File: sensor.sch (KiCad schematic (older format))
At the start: 74 parts, among them CON1 Micro USB, CON2 PROG, CON3 Jack-DC, CON4 HTU21D, CON5 N.C., Q1 BSS214N, Q2 BSS214N, Q3 BSS214N, SW1 RESET, SW2 CFG, U1 LM7805, U2 TLV1117LV33DCY, U3 ESP-12F, U4 HTU21D, U5 PMS7003

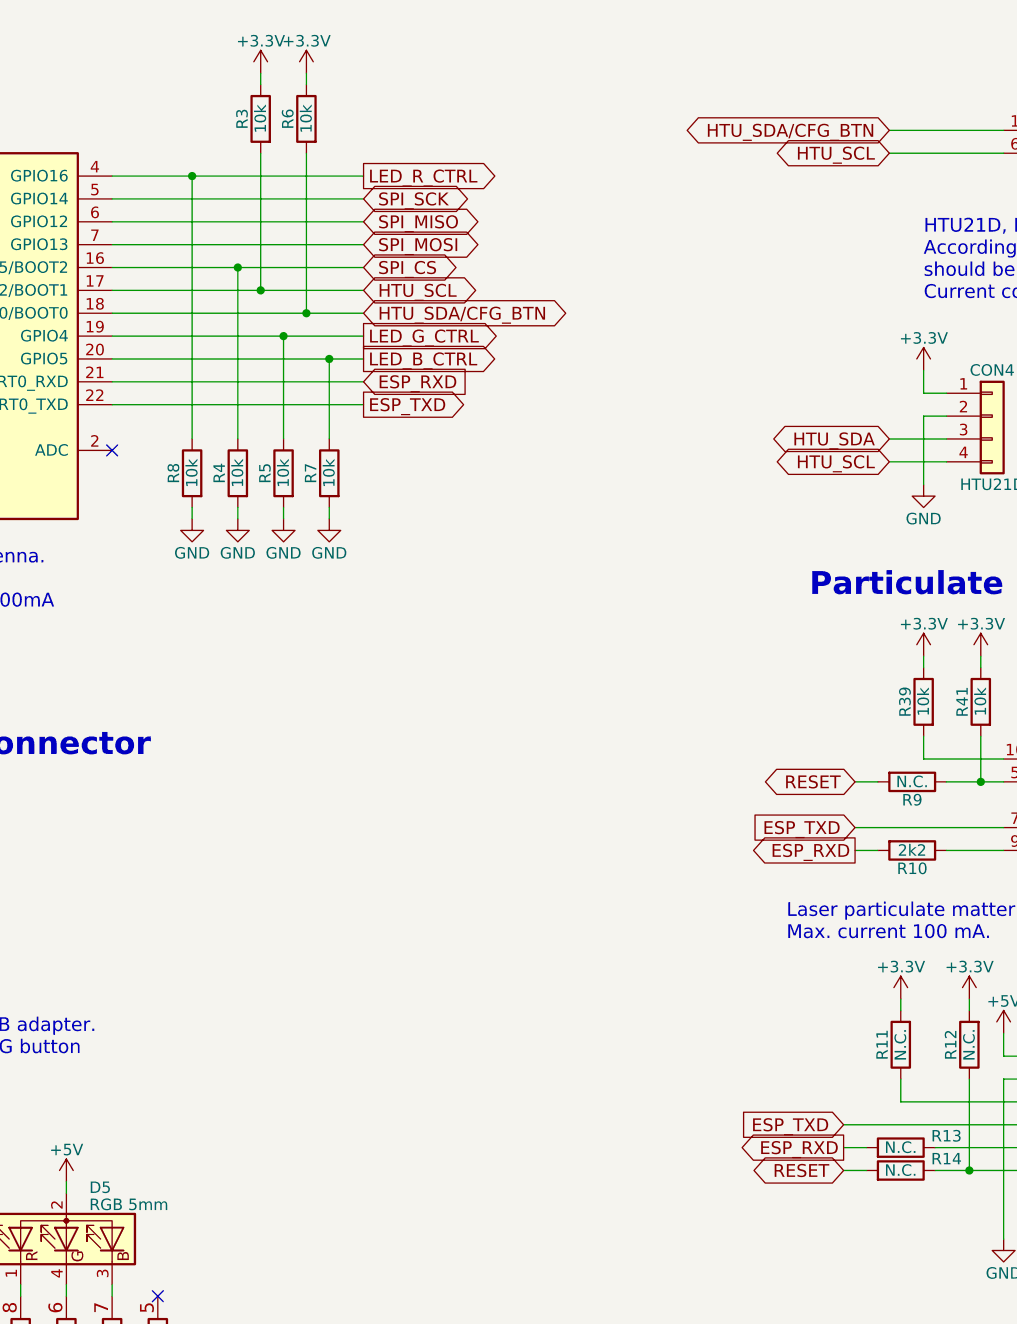
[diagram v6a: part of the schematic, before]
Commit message: Go back to previous ESP pinout, except I2C and LED_B_CTRL [#6] Hardware SPI for Lora module not available.
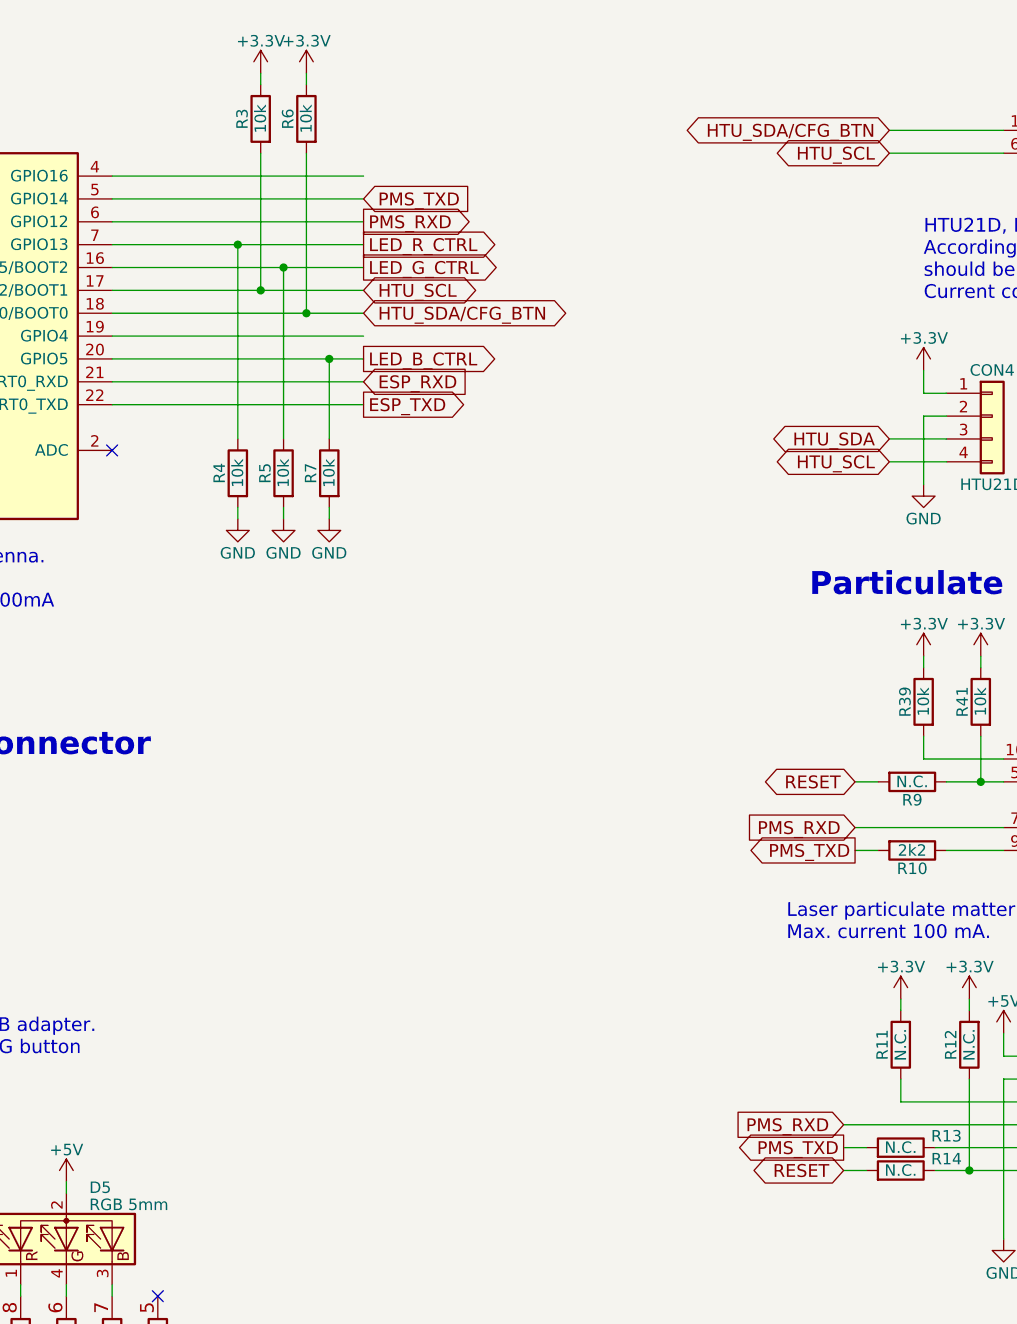
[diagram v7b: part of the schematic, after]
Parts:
- removed R8: 10k, less-smog:R_1206, symbol R
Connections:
- net SPI_MOSI is gone; now on net LED_R_CTRL: U3.7 (GPIO13)
- net ESP_RXD: no longer R10.2, R13.2
- net ESP_TXD: no longer CON5.4 (Pin_4), U5.7 (RX)
- net LED_G_CTRL: now also U3.16 (GPIO15/BOOT2); no longer U3.19 (GPIO4)
- net LED_R_CTRL: now also R4.1; no longer U3.4 (GPIO16)
- removed net SPI_CS: R4.1, U3.16 (GPIO15/BOOT2)
- net SPI_MISO renamed PMS_RXD
- net PMS_RXD: now also CON5.4 (Pin_4), U5.7 (RX)
- net SPI_SCK renamed PMS_TXD
- net PMS_TXD: now also R10.2, R13.2

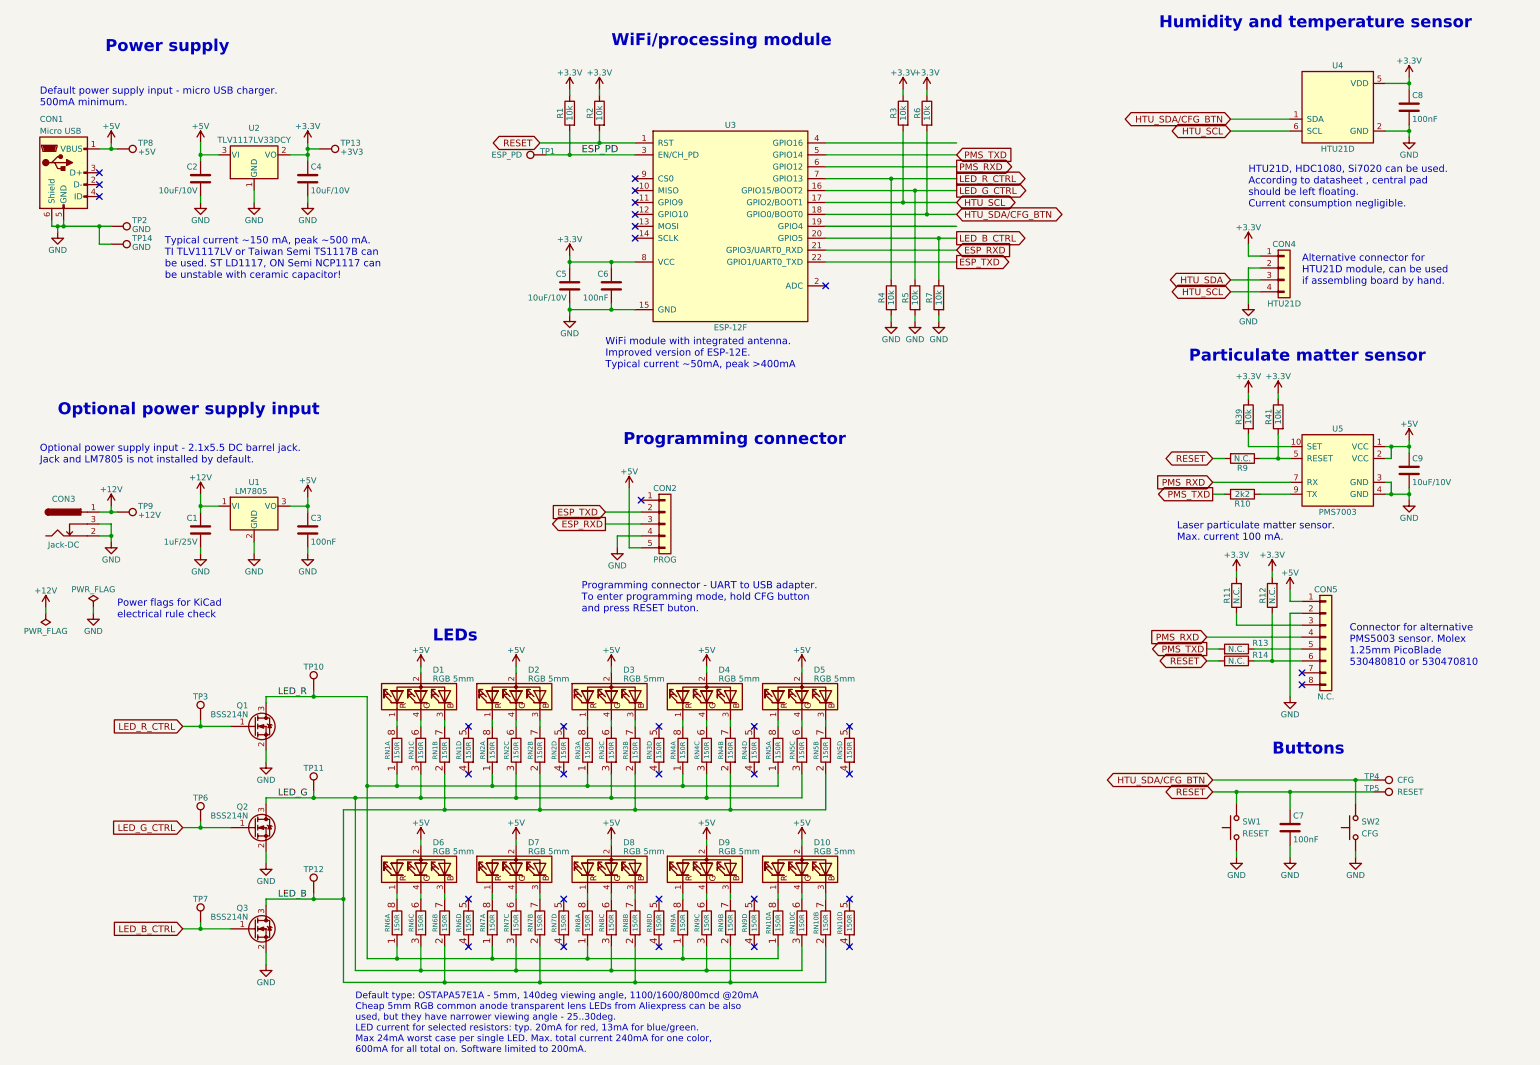
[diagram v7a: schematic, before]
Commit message: Change components to smaller ones. [#2] Change resistors to chip arrays.
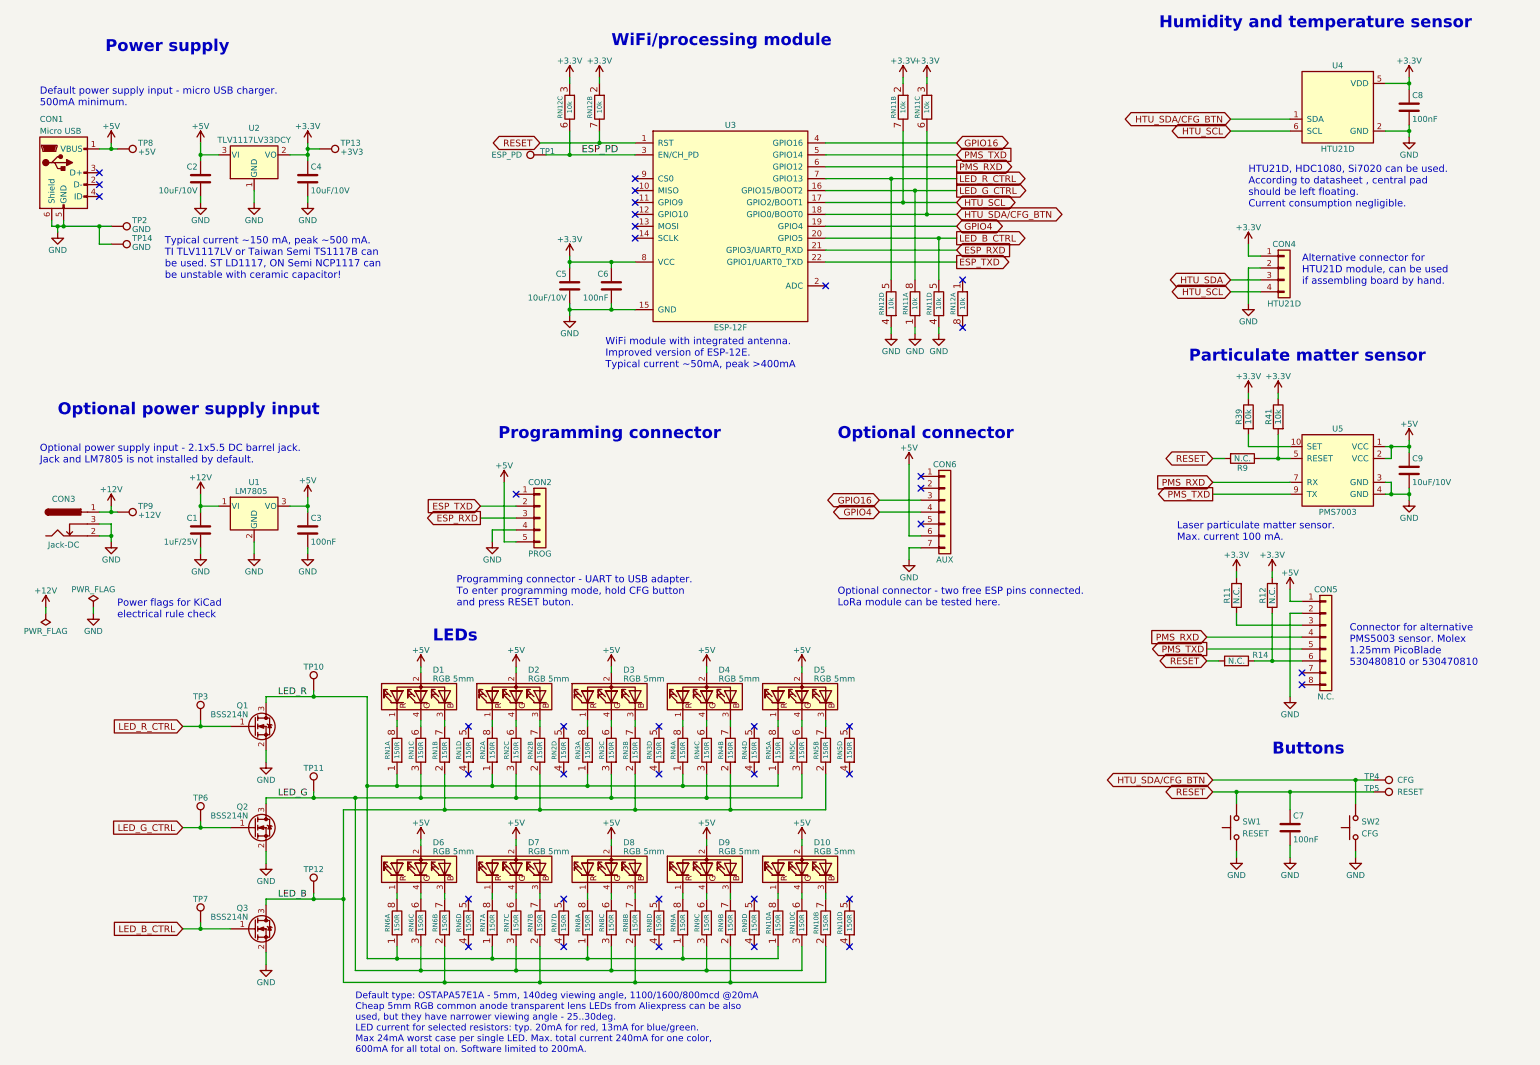
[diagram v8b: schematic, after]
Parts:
- removed R1, R2, R3, R4, R5, R6, R7: 10k, less-smog:R_1206, symbol R
- removed R10: 2k2, less-smog:R_1206, symbol R
- removed R13: N.C., less-smog:R_1206, symbol R
- added CON6: AUX, symbol Conn_01x07
- added RN11, RN12: 10k, less-smog:4x0402_M, symbol R_Network_4
- C3, C6, C7, C8: footprint less-smog:C_0805 -> less-smog:0603_M
- R11, R12, R14, R39, R41, R9: footprint less-smog:R_1206 -> less-smog:0603_R_M
- RN1, RN10, RN2, RN3, RN4, RN5, RN6, RN7, RN8, RN9: footprint 4x0603_N -> less-smog:4x0402_M
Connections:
- net +3V3: now also RN11.2 (1), RN11.3 (1), RN12.2 (1), RN12.3 (1)
- net +5V: now also CON6.6 (Pin_6)
- net ESP_PD: now also RN12.6 (2)
- net GND: now also CON6.7 (Pin_7), RN11.1, RN11.4 (1), RN12.4 (1)
- net HTU_SCL: now also RN11.7 (2)
- net HTU_SDA/CFG_BTN: now also RN11.6 (2)
- net LED_B_CTRL: now also RN11.5 (2)
- net LED_G_CTRL: now also RN11.8 (2)
- net LED_R_CTRL: now also RN12.5 (2)
- net PMS_TXD: now also CON5.5 (Pin_5), U5.9 (TX)
- net RESET: now also RN12.7 (2)
- net GPIO4: now reaches U3.19 (GPIO4)
- net GPIO4: now also CON6.4 (Pin_4)
- net GPIO16: now reaches U3.4 (GPIO16)
- net GPIO16: now also CON6.3 (Pin_3)
- no-connect marks 33 -> 38
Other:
- note added: "Optional connector"
- note added: "Optional connector - two free ESP pins connected.\nLoRa module can be tested here."
- moved on the sheet: CON2
